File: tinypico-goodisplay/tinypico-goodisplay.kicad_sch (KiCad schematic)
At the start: 34 parts, among them J1 AFC24-S24FIC-00, Q1 Si1308, U1 TinypicoESP32_Symbol, U2 PCF8563T, Y1 Crystal_Small

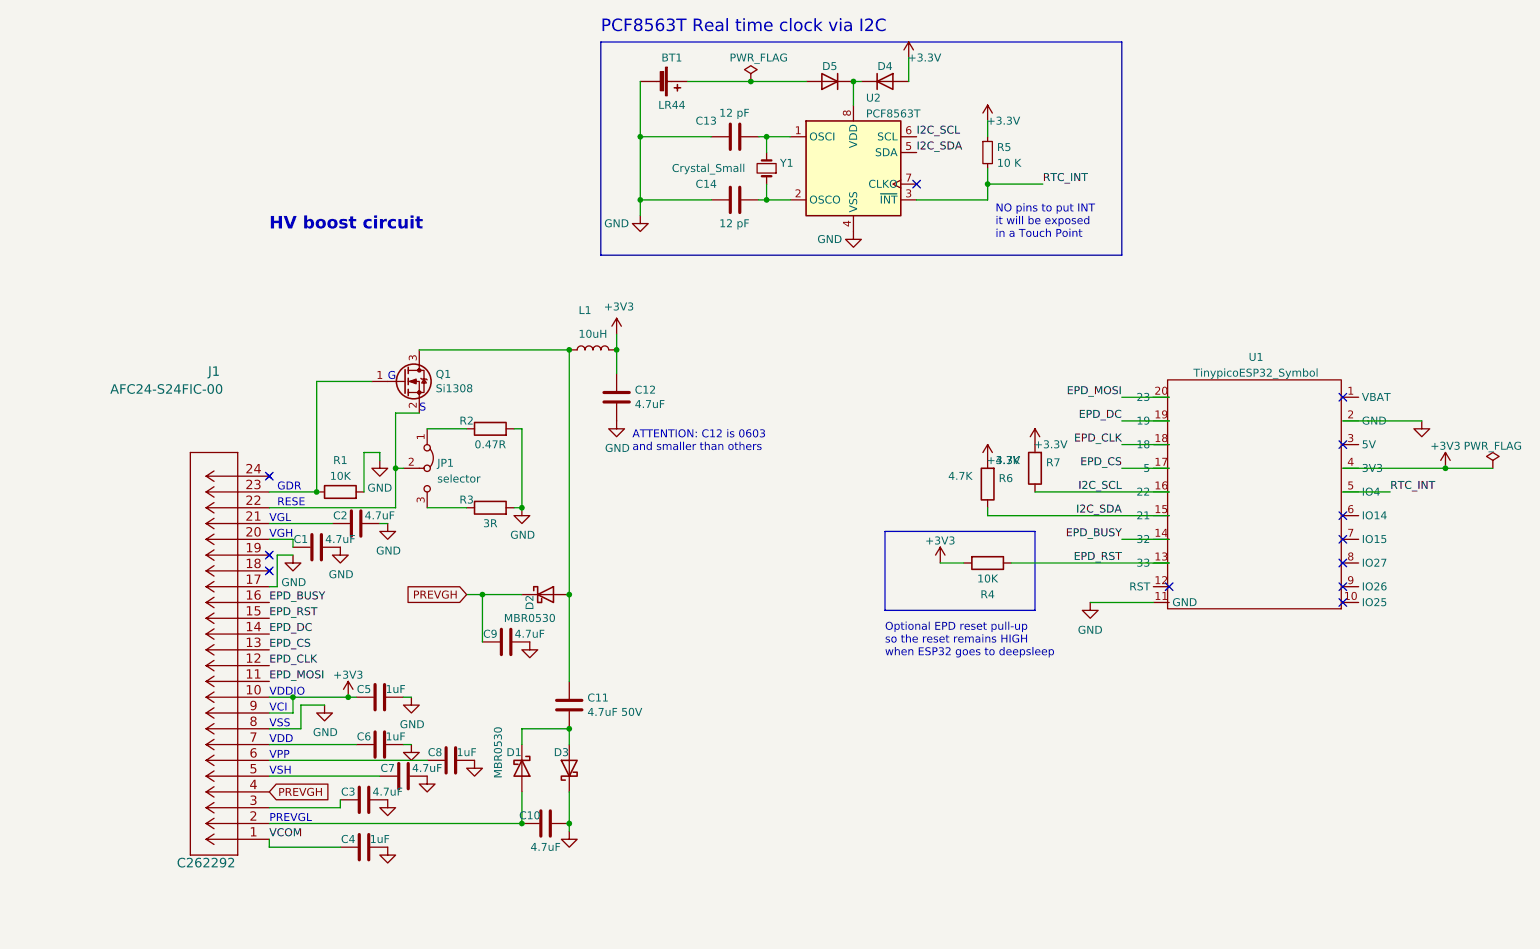
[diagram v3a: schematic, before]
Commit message: #2 Add CR1220 as optional RTC backup
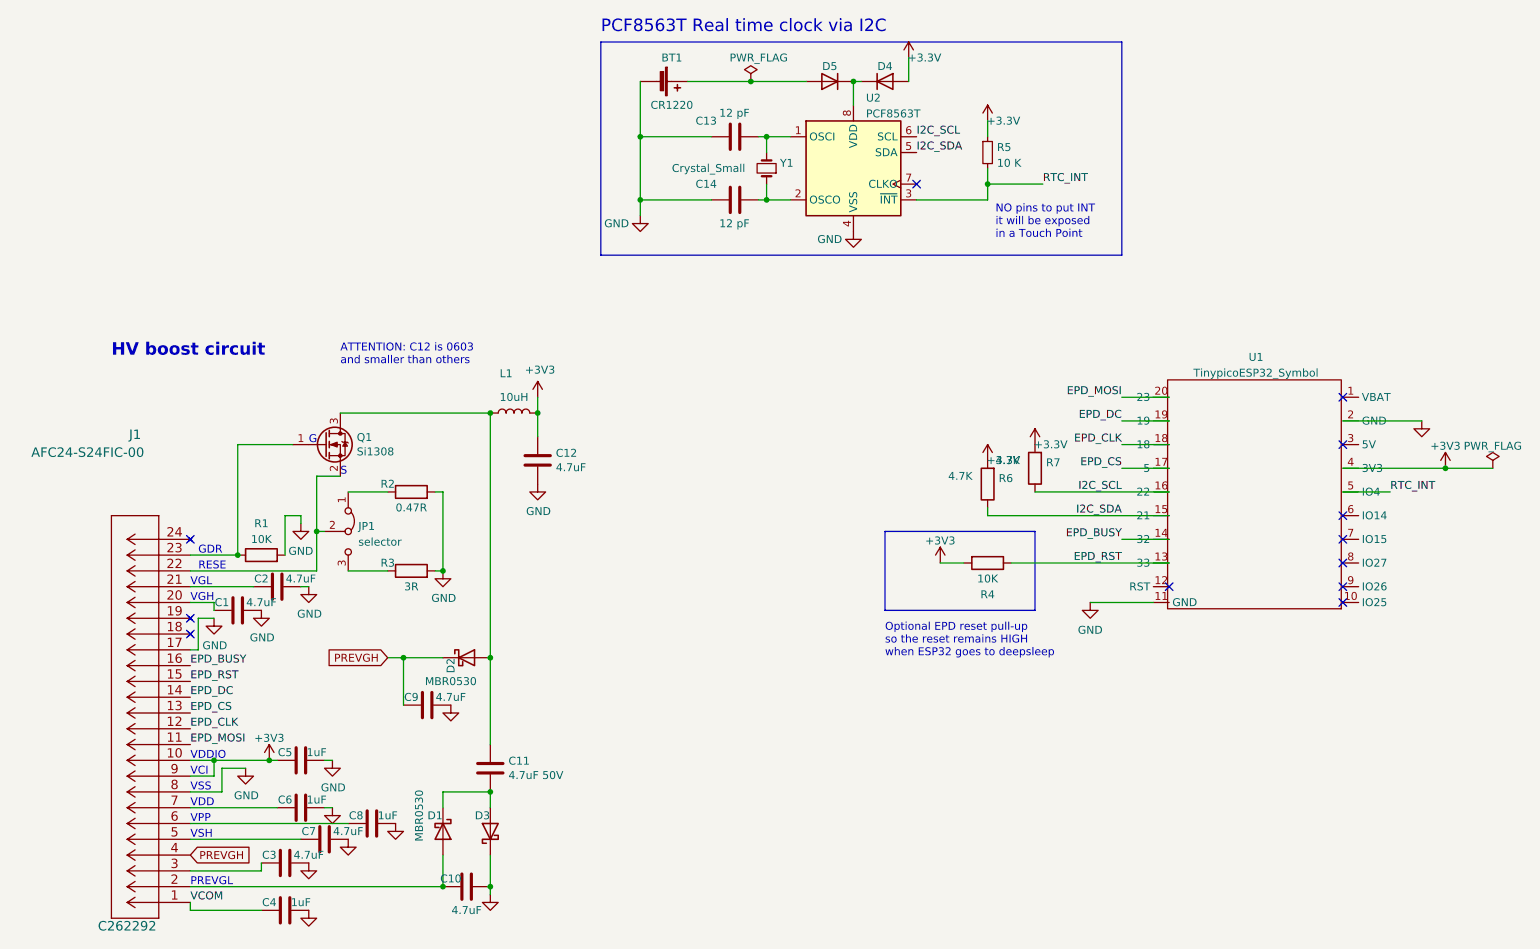
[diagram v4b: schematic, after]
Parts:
- BT1: value LR44 -> CR1220; footprint footprint:C964716_LR44 -> footprint:CR12202ZX; LCSC C964716 -> C969906
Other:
- moved on the sheet: C1, C10, C11, C12, C2, C3, C4, C5, C6, C7, C8, C9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

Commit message: Update SCH
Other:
- note added: "This are ESP32 IOs. Corresponding pins for S3 are in the PCB Silkscreen on the back"
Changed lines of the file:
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@@
     (effects (font (size 1.27 1.27)) (justify left bottom))
+  )
+  (text "This are ESP32 IOs. Corresponding pins for \nS3 are in the PCB Silkscreen on the back"
+    (at 199.39 68.58 0)
+    (effects (font (size 1.4 1.4)) (justify left bottom))
   )
   (text "S" (at 66.04 92.71 0)

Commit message: Add S3 AXE to 33 pin FPC Schematics
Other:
- note removed: "NO pins to put INT it will be exposed in a Touch Point"
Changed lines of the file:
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@@
-    (effects (font (size 1.27 1.27)) (justify left bottom))
-  )
-  (text "NO pins to put INT\nit will be exposed\nin a Touch Point"
-    (at 171.45 54.61 0)
     (effects (font (size 1.27 1.27)) (justify left bottom))
   )

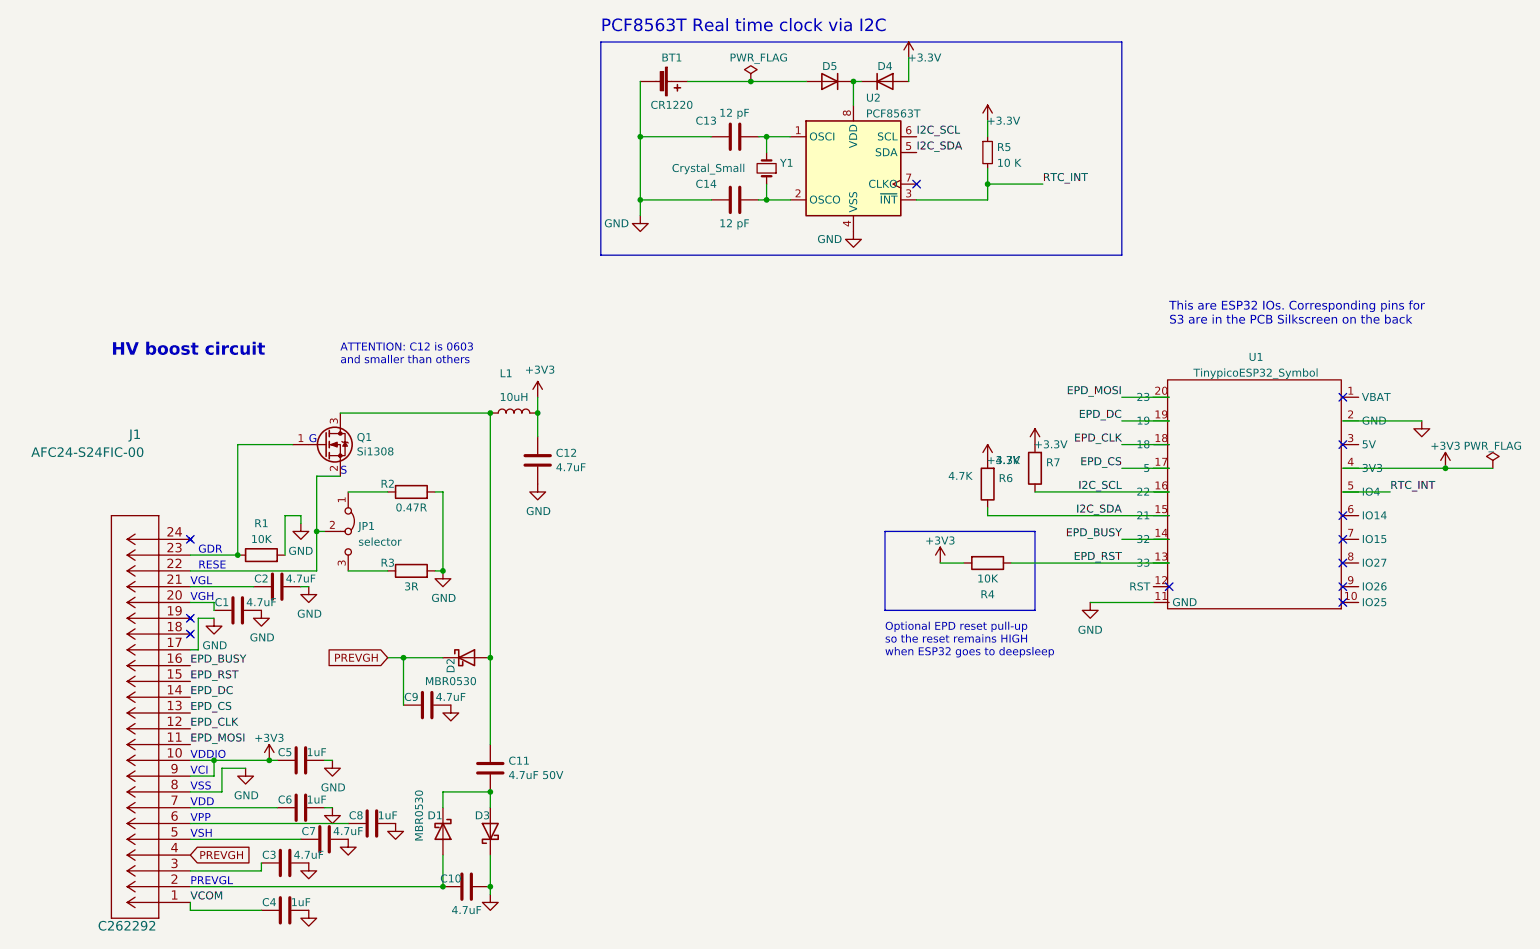
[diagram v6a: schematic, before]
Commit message: #3 Close this for Rev 1.1 220AC still has transistor Issues that need revision
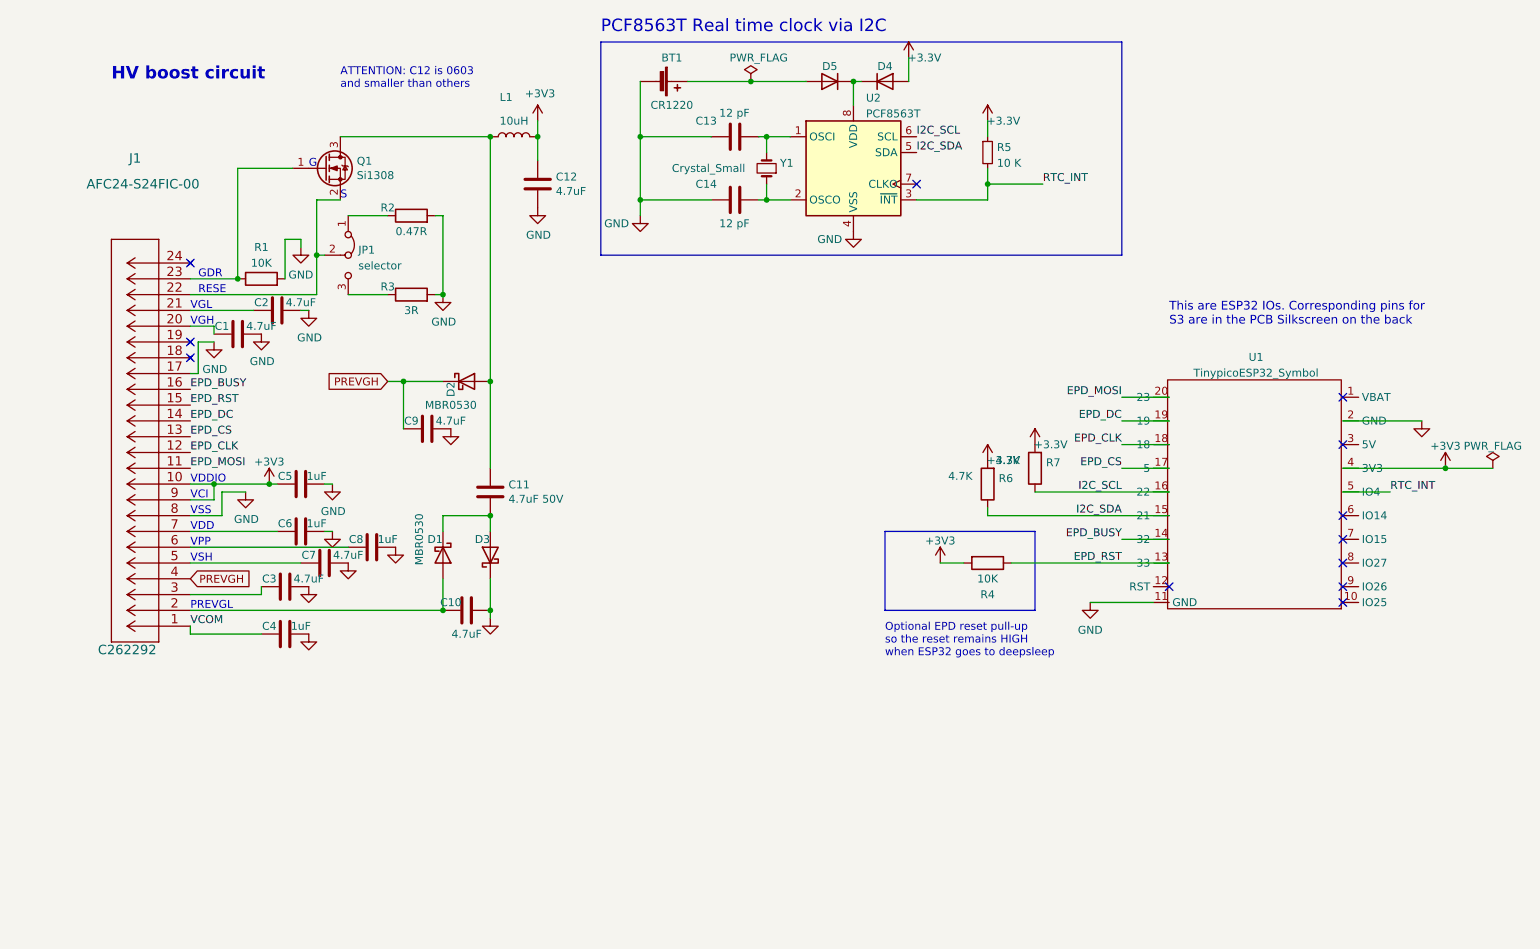
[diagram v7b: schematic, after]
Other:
- moved on the sheet: C1, C10, C11, C12, C2, C3, C4, C5, C6, C7, C8, C9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
